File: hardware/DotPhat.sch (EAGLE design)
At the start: 59 parts, among them CN1 1X4-BIG, IC1 CAT24M010TS, IC3 SI1145, J3 USB-MICROB, Q1 BSH103, U1 ATMEGA328P-MU-QFN32, U2 TMP102, U3 ATSHA204-TSU, U4 W25Q32FV, X2 MC-RTC-RV-4162-C7-I2C, X3 S4B-ZR

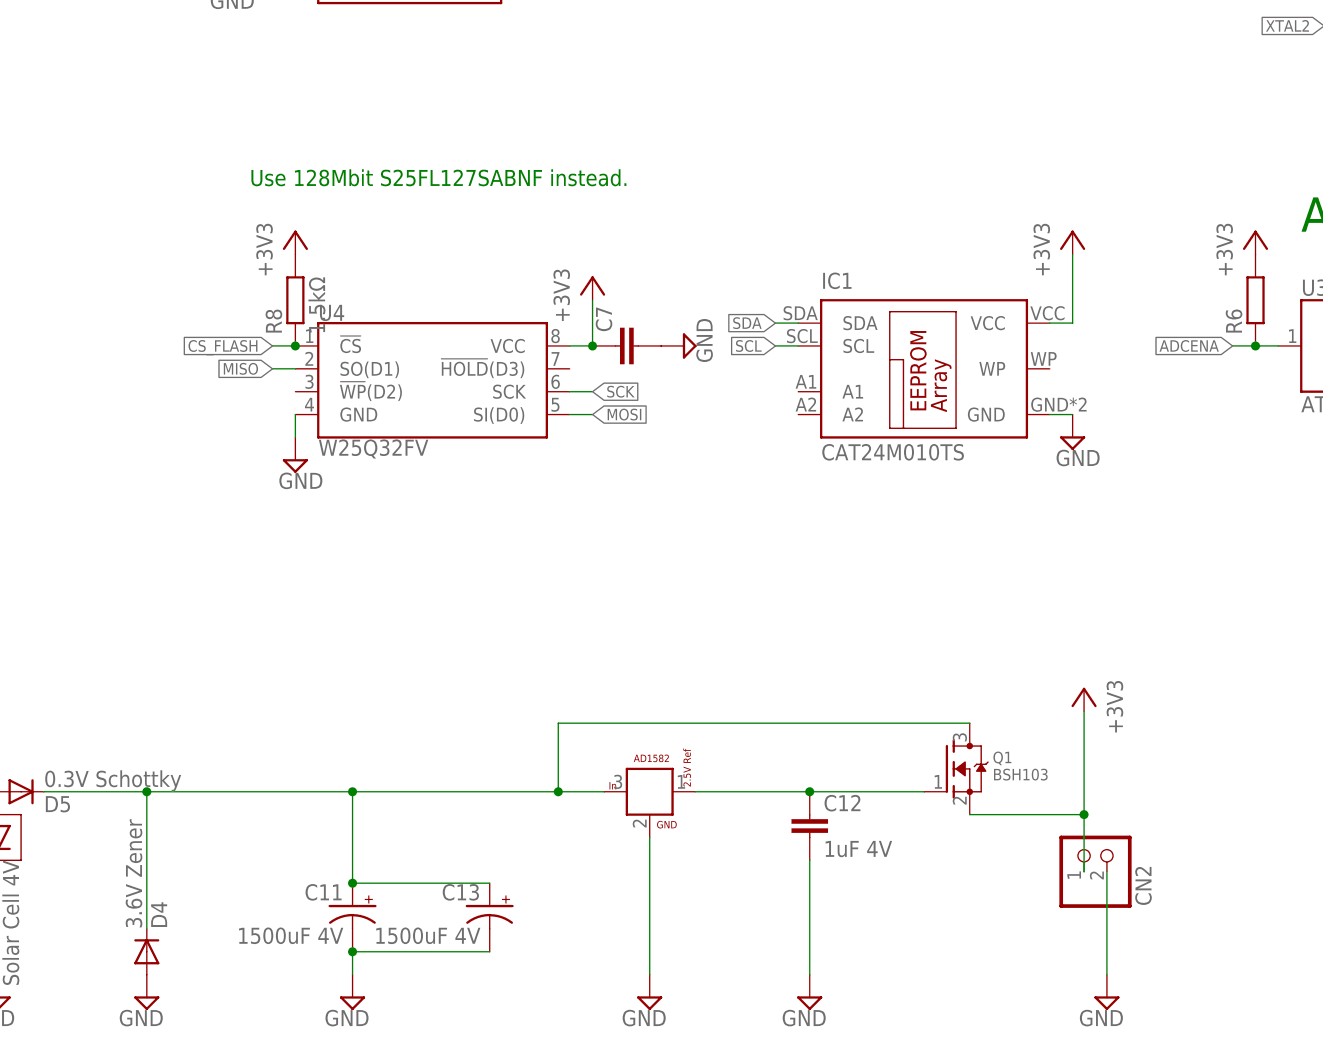
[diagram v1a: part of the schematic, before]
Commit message: Reroute signals after repositioning
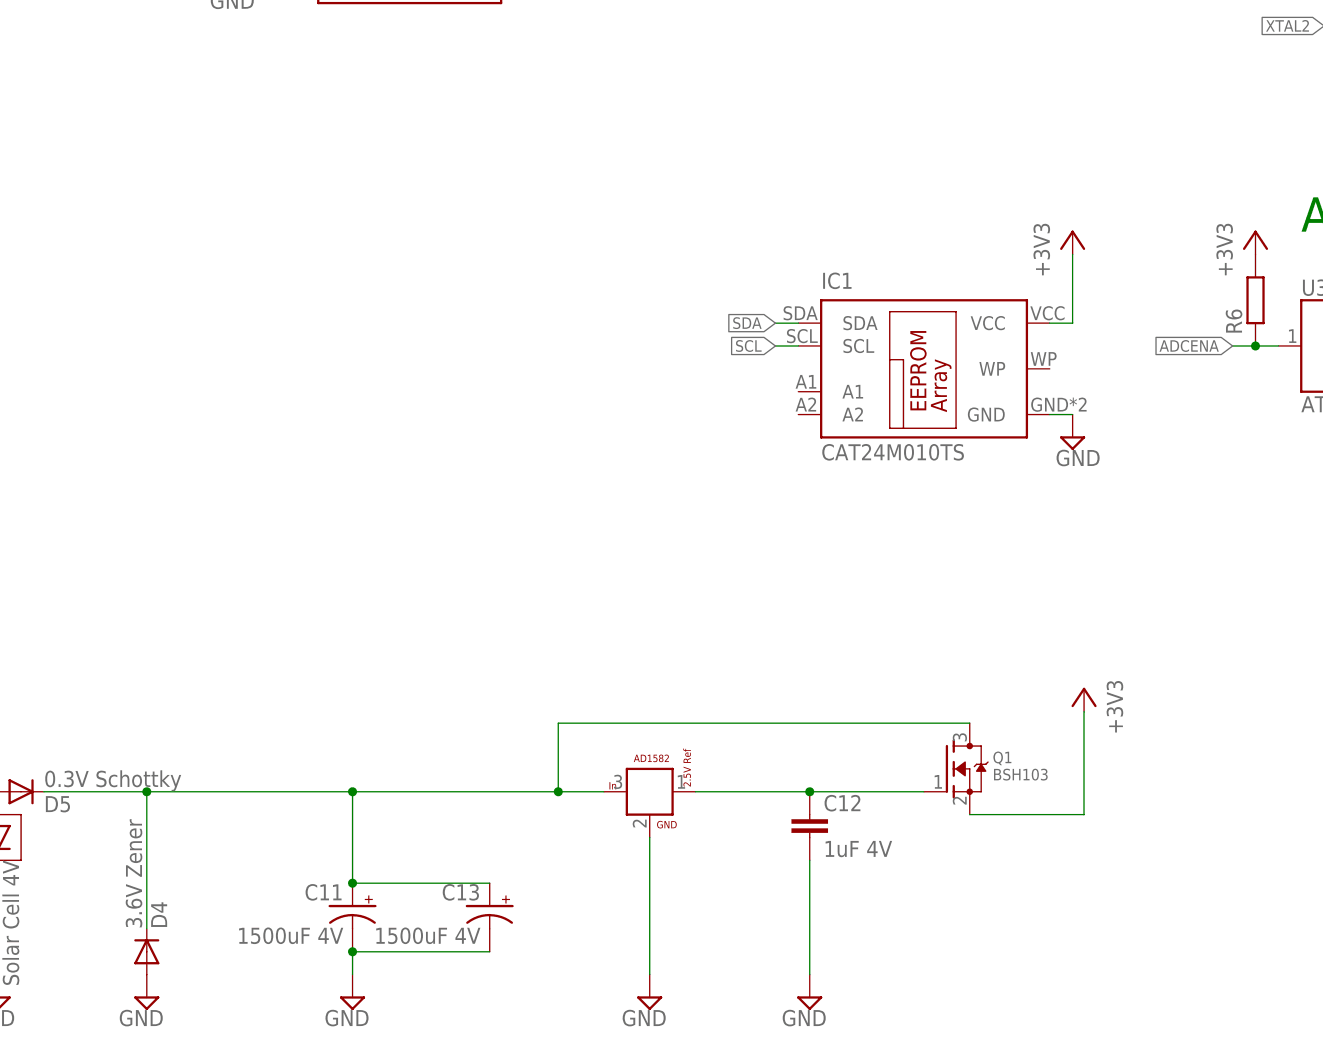
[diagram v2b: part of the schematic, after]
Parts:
- removed C7: (no value), rcl:C-EUC0603
- removed CN2: (no value), adafruit:JST_2PIN-SMT-RA
- removed R8: 1.5kΩ, rcl:R-EU_R0603
- removed U4: W25Q32FV, SparkFun-IC-Memory:W25Q32FVZP
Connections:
- net +3V3: no longer C7.1, CN2.2, R8.2, U4.VCC
- net CS_FLASH: no longer R8.1, U4.!CS!
- net GND: no longer C7.2, CN2.1, U4.GND
- net MISO: no longer U4.SO(D1)
- net MOSI: no longer U4.SI(D0)
- net SCK: no longer U4.SCK
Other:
- note removed: "Use 128Mbit S25FL127SABNF instead."
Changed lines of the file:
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@@
 <part name="JP4" library="SparkFun-Jumpers" deviceset="JUMPER-SMT_2_NC_TRACE" device="_NO-SILK"/>
 <part name="+3V16" library="supply1" deviceset="+3V3" device=""/>
-<part name="U4" library="SparkFun-IC-Memory" deviceset="W25Q32FV" device="ZP" value="W25Q32FV"/>
-<part name="+3V17" library="supply1" deviceset="+3V3" device=""/>
-<part name="SUPPLY23" library="supply2" deviceset="GND" device=""/>
-<part name="SUPPLY24" library="supply2" deviceset="GND" device=""/>
-<part name="C7" library="rcl" deviceset="C-EU" device="C0603"/>
-<part name="R8" library="rcl" deviceset="R-EU_" device="R0603" value="1.5kΩ"/>
-<part name="+3V18" library="supply1" deviceset="+3V3" device=""/>
 <part name="X2" library="Microcrystal-RTC" deviceset="MC-RTC-RV-4162-C7-I2C" device=""/>
 <part name="+3V20" library="supply1" deviceset="+3V3" device=""/>
@@
 <part name="+3V22" library="supply1" deviceset="+3V3" device=""/>
 <part name="SUPPLY36" library="supply2" deviceset="GND" device=""/>
-<part name="CN2" library="adafruit" deviceset="JST_2PIN" device="-SMT-RA"/>
-<part name="SUPPLY38" library="supply2" deviceset="GND" device=""/>
 <part name="D5" library="diode" deviceset="DIODE-" device="SOD523" value="0.3V Schottky"/>
 <part name="Q1" library="adafruit" deviceset="MOSFET-N" device="REFLOW" value="BSH103"/>
@@
 <text x="134.62" y="134.62" size="1.778" layer="91">white</text>
 <text x="134.62" y="124.46" size="1.778" layer="91">red</text>
-<text x="20.32" y="-142.24" size="1.778" layer="91">Use 128Mbit S25FL127SABNF instead.</text>
 <text x="25.4" y="-104.14" size="1.27" layer="91">Since nINT is conencted to CS_FLASH,
 special care when selecting the flash:
@@
 <instance part="JP4" gate="G$1" x="231.14" y="81.28"/>
 <instance part="+3V16" gate="G$1" x="254" y="-38.1"/>
-<instance part="U4" gate="G$1" x="40.64" y="-162.56"/>
-<instance part="+3V17" gate="G$1" x="58.42" y="-152.4"/>
-<instance part="SUPPLY23" gate="GND" x="25.4" y="-172.72"/>
-<instance part="SUPPLY24" gate="GND" x="68.58" y="-160.02" rot="R90"/>
-<instance part="C7" gate="G$1" x="60.96" y="-160.02" rot="R90"/>
-<instance part="R8" gate="G$1" x="25.4" y="-154.94" rot="R90"/>
-<instance part="+3V18" gate="G$1" x="25.4" y="-147.32"/>
 <instance part="X2" gate="G$1" x="38.1" y="-114.3"/>
 <instance part="+3V20" gate="G$1" x="73.66" y="-114.3"/>
@@
 <instance part="+3V22" gate="G$1" x="113.03" y="-198.12" rot="MR0"/>
 <instance part="SUPPLY36" gate="GND" x="82.55" y="-232.41" rot="MR0"/>
-<instance part="CN2" gate="G$1" x="113.03" y="-215.9" rot="MR90"/>
-<instance part="SUPPLY38" gate="GND" x="115.57" y="-232.41" rot="MR0"/>
 <instance part="D5" gate="G$1" x="-5.08" y="-209.55" rot="MR180"/>
 <instance part="Q1" gate="G$1" x="97.79" y="-207.01"/>
@@
 </segment>
 <segment>
-<pinref part="U4" gate="G$1" pin="GND"/>
-<pinref part="SUPPLY23" gate="GND" pin="GND"/>
-<wire x1="25.4" y1="-167.64" x2="25.4" y2="-170.18" width="0.1524" layer="91"/>
-</segment>
-<segment>
-<pinref part="SUPPLY24" gate="GND" pin="GND"/>
-<pinref part="C7" gate="G$1" pin="2"/>
-</segment>
-<segment>
 <pinref part="X2" gate="G$1" pin="GND"/>
 <pinref part="SUPPLY25" gate="GND" pin="GND"/>
@@
 <pinref part="C12" gate="G$1" pin="2"/>
 <wire x1="82.55" y1="-229.87" x2="82.55" y2="-217.17" width="0.1524" layer="91"/>
-</segment>
-<segment>
-<pinref part="SUPPLY38" gate="GND" pin="GND"/>
-<pinref part="CN2" gate="G$1" pin="1"/>
-<wire x1="115.57" y1="-229.87" x2="115.57" y2="-218.44" width="0.1524" layer="91"/>
 </segment>
 <segment>
@@
 </segment>
 <segment>
-<pinref part="U4" gate="G$1" pin="VCC"/>
-<pinref part="+3V17" gate="G$1" pin="+3V3"/>
-<wire x1="55.88" y1="-160.02" x2="58.42" y2="-160.02" width="0.1524" layer="91"/>
-<wire x1="58.42" y1="-160.02" x2="58.42" y2="-154.94" width="0.1524" layer="91"/>
-<pinref part="C7" gate="G$1" pin="1"/>
-<junction x="58.42" y="-160.02"/>
-</segment>
-<segment>
-<pinref part="R8" gate="G$1" pin="2"/>
-<pinref part="+3V18" gate="G$1" pin="+3V3"/>
-</segment>
-<segment>
 <pinref part="X2" gate="G$1" pin="VDD"/>
 <pinref part="+3V20" gate="G$1" pin="+3V3"/>
@@
 <segment>
 <pinref part="+3V22" gate="G$1" pin="+3V3"/>
-<pinref part="CN2" gate="G$1" pin="2"/>
-<wire x1="113.03" y1="-218.44" x2="113.03" y2="-212.09" width="0.1524" layer="91"/>
 <pinref part="Q1" gate="G$1" pin="S"/>
 <wire x1="113.03" y1="-212.09" x2="113.03" y2="-200.66" width="0.1524" layer="91"/>
 <wire x1="100.33" y1="-212.09" x2="113.03" y2="-212.09" width="0.1524" layer="91"/>
-<junction x="113.03" y="-212.09"/>
 </segment>
 <segment>
@@
 <label x="52.07" y="125.73" size="1.27" layer="95" rot="R180" xref="yes"/>
 </segment>
-<segment>
-<pinref part="U4" gate="G$1" pin="SI(D0)"/>
-<wire x1="55.88" y1="-167.64" x2="58.42" y2="-167.64" width="0.1524" layer="91"/>
-<label x="58.42" y="-167.64" size="1.27" layer="95" xref="yes"/>
-</segment>
 </net>
 <net name="MISO" class="0">
@@
 <label x="52.07" y="123.19" size="1.27" layer="95" rot="R180" xref="yes"/>
 </segment>
-<segment>
-<pinref part="U4" gate="G$1" pin="SO(D1)"/>
-<wire x1="25.4" y1="-162.56" x2="22.86" y2="-162.56" width="0.1524" layer="91"/>
-<label x="22.86" y="-162.56" size="1.27" layer="95" rot="R180" xref="yes"/>
-</segment>
 </net>
 <net name="TXD" class="0">
@@
 <wire x1="60.96" y1="120.65" x2="52.07" y2="120.65" width="0.1524" layer="91"/>
 <label x="52.07" y="120.65" size="1.27" layer="95" rot="R180" xref="yes"/>
-</segment>
-<segment>
-<pinref part="U4" gate="G$1" pin="SCK"/>
-<wire x1="55.88" y1="-165.1" x2="58.42" y2="-165.1" width="0.1524" layer="91"/>
-<label x="58.42" y="-165.1" size="1.27" layer="95" xref="yes"/>
 </segment>
 </net>
@@
 <net name="CS_FLASH" class="0">
 <segment>
-<pinref part="U4" gate="G$1" pin="!CS!"/>
-<pinref part="R8" gate="G$1" pin="1"/>
-<wire x1="25.4" y1="-160.02" x2="22.86" y2="-160.02" width="0.1524" layer="91"/>
-<junction x="25.4" y="-160.02"/>
-<label x="22.86" y="-160.02" size="1.27" layer="95" rot="R180" xref="yes"/>
-</segment>
-<segment>
 <pinref part="U1" gate="G$1" pin="PC0(ADC0/PCINT8)"/>

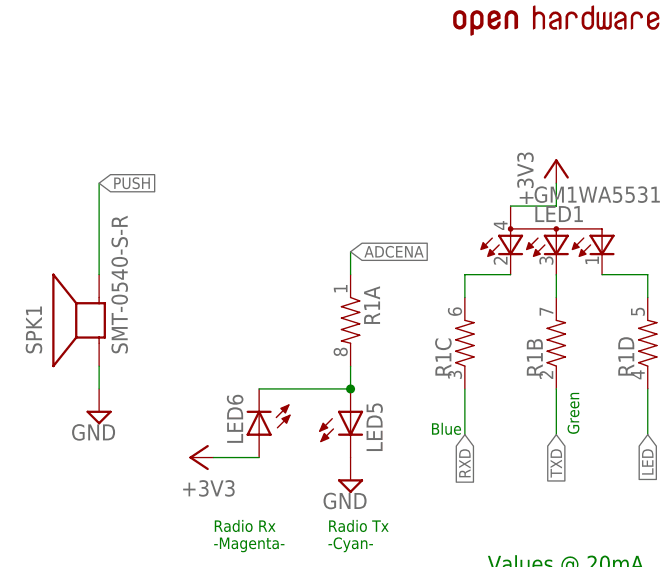
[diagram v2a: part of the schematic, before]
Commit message: Add TP for TRx leds
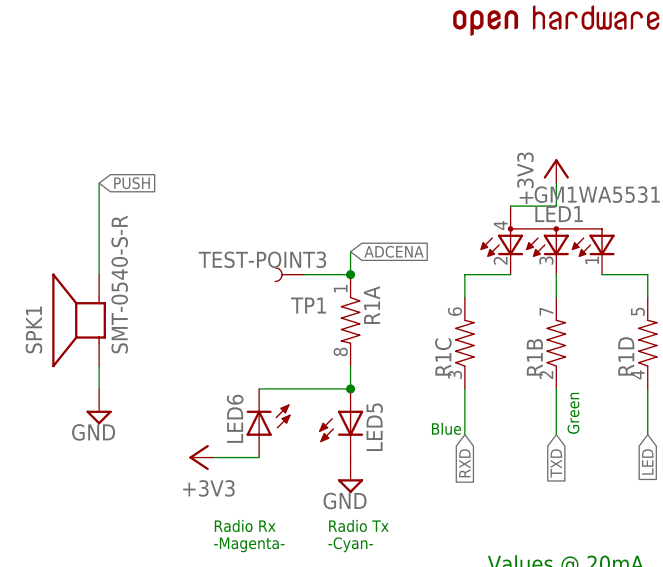
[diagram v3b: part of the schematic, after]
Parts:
- added TP1: TEST-POINT3, SparkFun:TEST-POINT3
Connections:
- net ADCENA: now also TP1.1
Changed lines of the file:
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@@
 <part name="SUPPLY37" library="supply2" deviceset="GND" device=""/>
 <part name="+3V23" library="supply1" deviceset="+3V3" device=""/>
+<part name="TP1" library="SparkFun" deviceset="TEST-POINT" device="3"/>
 </parts>
 <sheets>
@@
 <instance part="SUPPLY37" gate="GND" x="170.18" y="-228.6" rot="MR0"/>
 <instance part="+3V23" gate="G$1" x="149.86" y="-203.2"/>
+<instance part="TP1" gate="G$1" x="-50.8" y="68.58" rot="R180"/>
 </instances>
 <busses>
@@
 <wire x1="-45.72" y1="68.58" x2="-45.72" y2="71.12" width="0.1524" layer="91"/>
 <label x="-45.72" y="71.12" size="1.27" layer="95" xref="yes"/>
-</segment>
-</net>
+<pinref part="TP1" gate="G$1" pin="1"/>
+<wire x1="-50.8" y1="68.58" x2="-45.72" y2="68.58" width="0.1524" layer="91"/>
+<junction x="-45.72" y="68.58"/>
+</segment>
+</net>

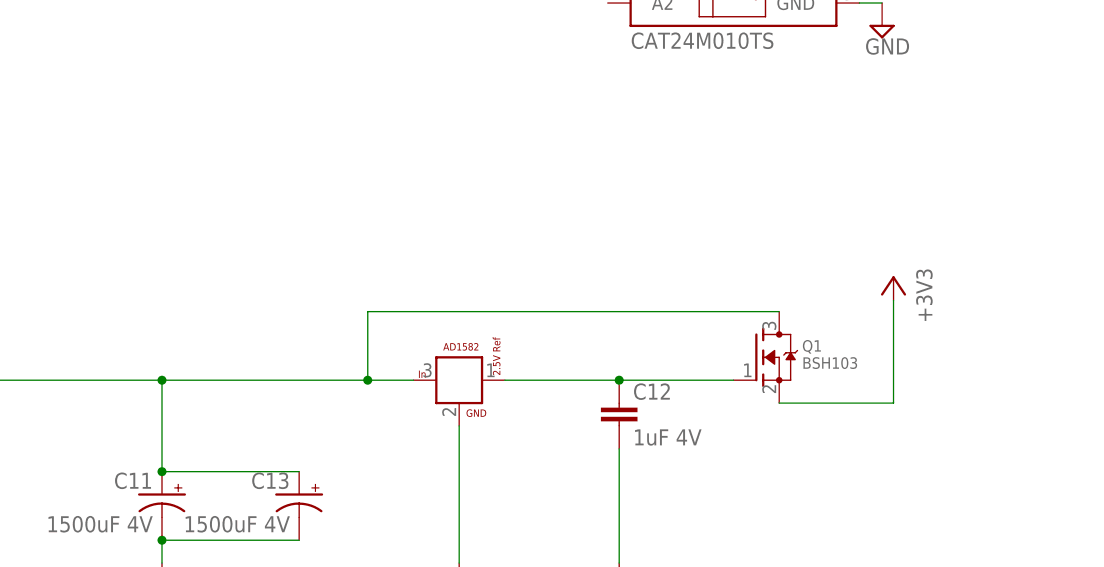
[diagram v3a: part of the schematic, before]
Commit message: Add SJ for bypass threshold VCC, polarity markers
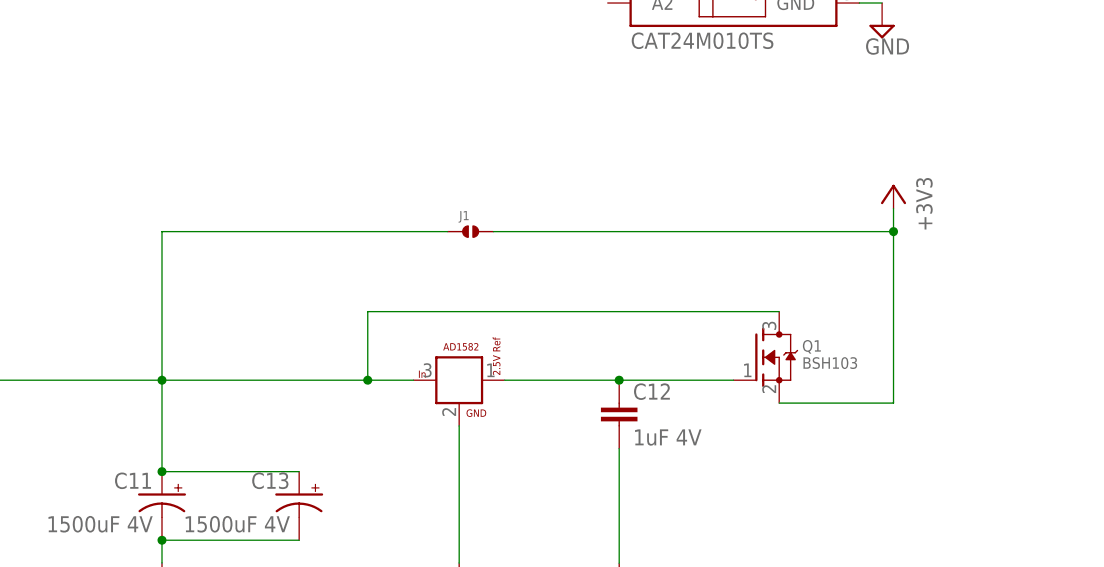
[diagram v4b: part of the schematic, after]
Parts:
- added J1: (no value), solderjumper:SOLDERJUMPER.2.MED
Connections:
- net +3V3: now also J1.2
- net CAPS_VCC: now also J1.1
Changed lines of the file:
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@@
 <setting verticaltext="up"/>
 </settings>
-<grid distance="0.1" unitdist="inch" unit="inch" style="lines" multiple="1" display="no" altdistance="0.01" altunitdist="inch" altunit="inch"/>
+<grid distance="0.05" unitdist="inch" unit="inch" style="lines" multiple="1" display="no" altdistance="0.01" altunitdist="inch" altunit="inch"/>
 <layers>
 <layer number="1" name="Top" color="4" fill="1" visible="no" active="no"/>
@@
 <part name="+3V23" library="supply1" deviceset="+3V3" device=""/>
 <part name="TP1" library="SparkFun" deviceset="TEST-POINT" device="3"/>
+<part name="J1" library="solderjumper" deviceset="SOLDERJUMPER.2" device=".MED"/>
 </parts>
 <sheets>
@@
 <instance part="C13" gate="G$1" x="46.99" y="-222.25" rot="MR0"/>
 <instance part="SUPPLY34" gate="GND" x="8.89" y="-232.41" rot="MR0"/>
-<instance part="+3V22" gate="G$1" x="113.03" y="-198.12" rot="MR0"/>
+<instance part="+3V22" gate="G$1" x="113.03" y="-187.96" rot="MR0"/>
 <instance part="SUPPLY36" gate="GND" x="82.55" y="-232.41" rot="MR0"/>
 <instance part="D5" gate="G$1" x="-5.08" y="-209.55" rot="MR180"/>
@@
 <instance part="+3V23" gate="G$1" x="149.86" y="-203.2"/>
 <instance part="TP1" gate="G$1" x="-50.8" y="68.58" rot="R180"/>
+<instance part="J1" gate="G$1" x="66.04" y="-193.04"/>
 </instances>
 <busses>
@@
 <pinref part="+3V22" gate="G$1" pin="+3V3"/>
 <pinref part="Q1" gate="G$1" pin="S"/>
-<wire x1="113.03" y1="-212.09" x2="113.03" y2="-200.66" width="0.1524" layer="91"/>
+<wire x1="113.03" y1="-212.09" x2="113.03" y2="-193.04" width="0.1524" layer="91"/>
+<wire x1="113.03" y1="-193.04" x2="113.03" y2="-190.5" width="0.1524" layer="91"/>
 <wire x1="100.33" y1="-212.09" x2="113.03" y2="-212.09" width="0.1524" layer="91"/>
+<pinref part="J1" gate="G$1" pin="2"/>
+<wire x1="68.58" y1="-193.04" x2="113.03" y2="-193.04" width="0.1524" layer="91"/>
+<junction x="113.03" y="-193.04"/>
 </segment>
 <segment>
@@
 <wire x1="54.61" y1="-201.93" x2="54.61" y2="-209.55" width="0.1524" layer="91"/>
 <junction x="54.61" y="-209.55"/>
-</segment>
-</net>
+<pinref part="J1" gate="G$1" pin="1"/>
+<wire x1="63.5" y1="-193.04" x2="31.75" y2="-193.04" width="0.1524" layer="91"/>
+<wire x1="31.75" y1="-193.04" x2="31.75" y2="-209.55" width="0.1524" layer="91"/>
+</segment>
+</net>
